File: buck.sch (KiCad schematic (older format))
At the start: 11 parts, among them U2 MP2467

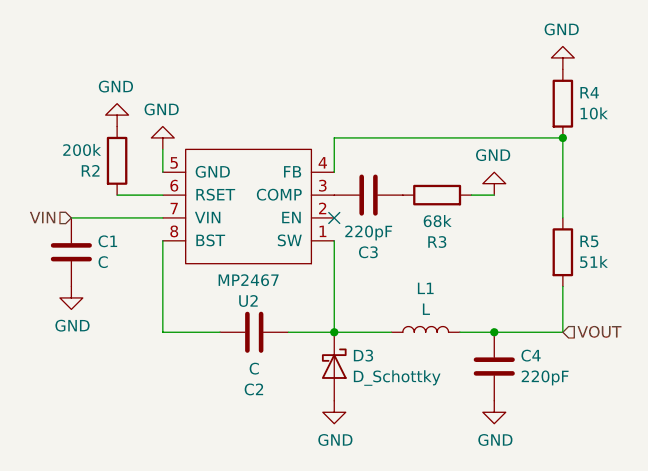
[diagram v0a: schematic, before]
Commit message: Batteries done and raspi added
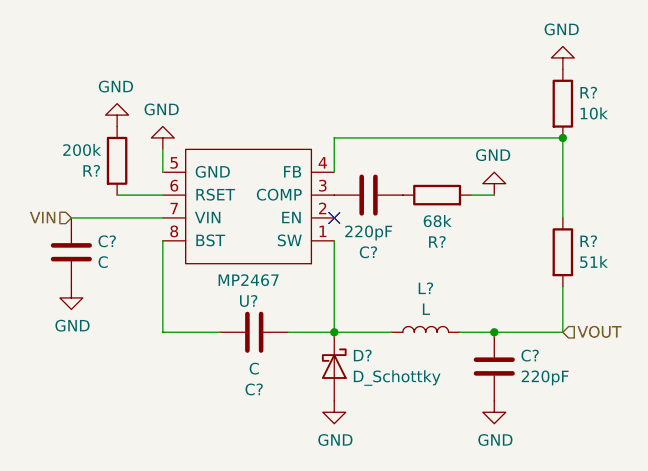
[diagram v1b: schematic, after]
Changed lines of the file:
@@
 $Descr A4 11693 8268
 encoding utf-8
-Sheet 2 7
+Sheet 2 14
 Title ""
 Date ""
@@
 AR Path="/5BDB6444/5BDB68AC" Ref="U2"  Part="1"
 AR Path="/5BE5CA5D/5BDB68AC" Ref="U?"  Part="1"
-F 0 "U2" H 5775 3915 50  0000 C CNN
+AR Path="/5C45D14E/5BDB68AC" Ref="U?"  Part="1"
+F 0 "U?" H 5775 3915 50  0000 C CNN
 F 1 "MP2467" H 5775 3824 50  0000 C CNN
 F 2 "" H 5750 3800 50  0001 C CNN
@@
 AR Path="/5BDB6444/5BDB68B3" Ref="#PWR08"  Part="1"
 AR Path="/5BE5CA5D/5BDB68B3" Ref="#PWR?"  Part="1"
-F 0 "#PWR08" H 4450 3000 50  0001 C CNN
+AR Path="/5C45D14E/5BDB68B3" Ref="#PWR?"  Part="1"
+F 0 "#PWR?" H 4450 3000 50  0001 C CNN
 F 1 "GND" H 4455 3077 50  0000 C CNN
 F 2 "" H 4450 3250 50  0001 C CNN
@@
 AR Path="/5BDB6444/5BDB68B9" Ref="C2"  Part="1"
 AR Path="/5BE5CA5D/5BDB68B9" Ref="C?"  Part="1"
-F 0 "C2" V 4598 4050 50  0000 C CNN
+AR Path="/5C45D14E/5BDB68B9" Ref="C?"  Part="1"
+F 0 "C?" V 4598 4050 50  0000 C CNN
 F 1 "C" V 4689 4050 50  0000 C CNN
 F 2 "" H 4888 3900 50  0001 C CNN
@@
 AR Path="/5BDB6444/5BDB68C4" Ref="C1"  Part="1"
 AR Path="/5BE5CA5D/5BDB68C4" Ref="C?"  Part="1"
-F 0 "C1" H 4165 3746 50  0000 L CNN
+AR Path="/5C45D14E/5BDB68C4" Ref="C?"  Part="1"
+F 0 "C?" H 4165 3746 50  0000 L CNN
 F 1 "C" H 4165 3655 50  0000 L CNN
 F 2 "" H 4088 3550 50  0001 C CNN
@@
 AR Path="/5BDB6444/5BDB68CB" Ref="#PWR06"  Part="1"
 AR Path="/5BE5CA5D/5BDB68CB" Ref="#PWR?"  Part="1"
-F 0 "#PWR06" H 4050 3600 50  0001 C CNN
+AR Path="/5C45D14E/5BDB68CB" Ref="#PWR?"  Part="1"
+F 0 "#PWR?" H 4050 3600 50  0001 C CNN
 F 1 "GND" H 4055 3677 50  0000 C CNN
 F 2 "" H 4050 3850 50  0001 C CNN
@@
 AR Path="/5BDB6444/5BDB68D2" Ref="C3"  Part="1"
 AR Path="/5BE5CA5D/5BDB68D2" Ref="C?"  Part="1"
-F 0 "C3" V 5098 3450 50  0000 C CNN
+AR Path="/5C45D14E/5BDB68D2" Ref="C?"  Part="1"
+F 0 "C?" V 5098 3450 50  0000 C CNN
 F 1 "220pF" V 5189 3450 50  0000 C CNN
 F 2 "" H 5388 3300 50  0001 C CNN
@@
 AR Path="/5BDB6444/5BDB68D9" Ref="R3"  Part="1"
 AR Path="/5BE5CA5D/5BDB68D9" Ref="R?"  Part="1"
-F 0 "R3" V 5443 3450 50  0000 C CNN
+AR Path="/5C45D14E/5BDB68D9" Ref="R?"  Part="1"
+F 0 "R?" V 5443 3450 50  0000 C CNN
 F 1 "68k" V 5534 3450 50  0000 C CNN
 F 2 "" V 5580 3450 50  0001 C CNN
@@
 AR Path="/5BDB6444/5BDB68E0" Ref="#PWR010"  Part="1"
 AR Path="/5BE5CA5D/5BDB68E0" Ref="#PWR?"  Part="1"
-F 0 "#PWR010" H 5900 3200 50  0001 C CNN
+AR Path="/5C45D14E/5BDB68E0" Ref="#PWR?"  Part="1"
+F 0 "#PWR?" H 5900 3200 50  0001 C CNN
 F 1 "GND" H 5905 3277 50  0000 C CNN
 F 2 "" H 5900 3450 50  0001 C CNN
@@
 AR Path="/5BDB6444/5BDB68E7" Ref="R2"  Part="1"
 AR Path="/5BE5CA5D/5BDB68E7" Ref="R?"  Part="1"
-F 0 "R2" H 4180 3254 50  0000 R CNN
+AR Path="/5C45D14E/5BDB68E7" Ref="R?"  Part="1"
+F 0 "R?" H 4180 3254 50  0000 R CNN
 F 1 "200k" H 4180 3345 50  0000 R CNN
 F 2 "" V 4180 3300 50  0001 C CNN
@@
 AR Path="/5BDB6444/5BDB68EF" Ref="#PWR07"  Part="1"
 AR Path="/5BE5CA5D/5BDB68EF" Ref="#PWR?"  Part="1"
-F 0 "#PWR07" H 4250 2900 50  0001 C CNN
+AR Path="/5C45D14E/5BDB68EF" Ref="#PWR?"  Part="1"
+F 0 "#PWR?" H 4250 2900 50  0001 C CNN
 F 1 "GND" H 4255 2977 50  0000 C CNN
 F 2 "" H 4250 3150 50  0001 C CNN
@@
 AR Path="/5BDB6444/5BDB68F6" Ref="D3"  Part="1"
 AR Path="/5BE5CA5D/5BDB68F6" Ref="D?"  Part="1"
-F 0 "D3" V 5154 4279 50  0000 L CNN
+AR Path="/5C45D14E/5BDB68F6" Ref="D?"  Part="1"
+F 0 "D?" V 5154 4279 50  0000 L CNN
 F 1 "D_Schottky" V 5245 4279 50  0000 L CNN
 F 2 "" H 5200 4200 50  0001 C CNN
@@
 AR Path="/5BDB6444/5BDB68FE" Ref="#PWR09"  Part="1"
 AR Path="/5BE5CA5D/5BDB68FE" Ref="#PWR?"  Part="1"
-F 0 "#PWR09" H 5200 4100 50  0001 C CNN
+AR Path="/5C45D14E/5BDB68FE" Ref="#PWR?"  Part="1"
+F 0 "#PWR?" H 5200 4100 50  0001 C CNN
 F 1 "GND" H 5205 4177 50  0000 C CNN
 F 2 "" H 5200 4350 50  0001 C CNN
@@
 AR Path="/5BDB6444/5BDB6904" Ref="L1"  Part="1"
 AR Path="/5BE5CA5D/5BDB6904" Ref="L?"  Part="1"
-F 0 "L1" V 5790 4050 50  0000 C CNN
+AR Path="/5C45D14E/5BDB6904" Ref="L?"  Part="1"
+F 0 "L?" V 5790 4050 50  0000 C CNN
 F 1 "L" V 5699 4050 50  0000 C CNN
 F 2 "" H 5600 4050 50  0001 C CNN
@@
 AR Path="/5BDB6444/5BDB690C" Ref="C4"  Part="1"
 AR Path="/5BE5CA5D/5BDB690C" Ref="C?"  Part="1"
-F 0 "C4" H 6015 4246 50  0000 L CNN
+AR Path="/5C45D14E/5BDB690C" Ref="C?"  Part="1"
+F 0 "C?" H 6015 4246 50  0000 L CNN
 F 1 "220pF" H 6015 4155 50  0000 L CNN
 F 2 "" H 5938 4050 50  0001 C CNN
@@
 AR Path="/5BDB6444/5BDB6913" Ref="#PWR011"  Part="1"
 AR Path="/5BE5CA5D/5BDB6913" Ref="#PWR?"  Part="1"
-F 0 "#PWR011" H 5900 4100 50  0001 C CNN
+AR Path="/5C45D14E/5BDB6913" Ref="#PWR?"  Part="1"
+F 0 "#PWR?" H 5900 4100 50  0001 C CNN
 F 1 "GND" H 5905 4177 50  0000 C CNN
 F 2 "" H 5900 4350 50  0001 C CNN
@@
 AR Path="/5BDB6444/5BDB691A" Ref="R5"  Part="1"
 AR Path="/5BE5CA5D/5BDB691A" Ref="R?"  Part="1"
-F 0 "R5" H 6270 3746 50  0000 L CNN
+AR Path="/5C45D14E/5BDB691A" Ref="R?"  Part="1"
+F 0 "R?" H 6270 3746 50  0000 L CNN
 F 1 "51k" H 6270 3655 50  0000 L CNN
 F 2 "" V 6130 3700 50  0001 C CNN
@@
 AR Path="/5BDB6444/5BDB6921" Ref="R4"  Part="1"
 AR Path="/5BE5CA5D/5BDB6921" Ref="R?"  Part="1"
-F 0 "R4" H 6270 3096 50  0000 L CNN
+AR Path="/5C45D14E/5BDB6921" Ref="R?"  Part="1"
+F 0 "R?" H 6270 3096 50  0000 L CNN
 F 1 "10k" H 6270 3005 50  0000 L CNN
 F 2 "" V 6130 3050 50  0001 C CNN
@@
 AR Path="/5BDB6444/5BDB692F" Ref="#PWR012"  Part="1"
 AR Path="/5BE5CA5D/5BDB692F" Ref="#PWR?"  Part="1"
-F 0 "#PWR012" H 6200 2650 50  0001 C CNN
+AR Path="/5C45D14E/5BDB692F" Ref="#PWR?"  Part="1"
+F 0 "#PWR?" H 6200 2650 50  0001 C CNN
 F 1 "GND" H 6205 2727 50  0000 C CNN
 F 2 "" H 6200 2900 50  0001 C CNN

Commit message: Schematics Done. Now need to do footprints
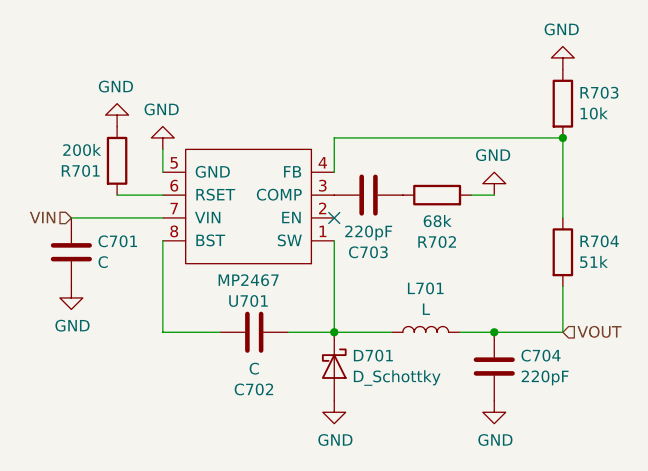
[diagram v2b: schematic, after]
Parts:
- R2, R3, R4, R5: footprint (none) -> Resistor_SMD:R_0805_2012Metric
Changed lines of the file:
@@
 AR Path="/5BDB6444/5BDB68AC" Ref="U2"  Part="1"
 AR Path="/5BE5CA5D/5BDB68AC" Ref="U?"  Part="1"
-AR Path="/5C45D14E/5BDB68AC" Ref="U?"  Part="1"
-F 0 "U?" H 5775 3915 50  0000 C CNN
+AR Path="/5C45D14E/5BDB68AC" Ref="U701"  Part="1"
+F 0 "U701" H 5775 3915 50  0000 C CNN
 F 1 "MP2467" H 5775 3824 50  0000 C CNN
 F 2 "" H 5750 3800 50  0001 C CNN
@@
 AR Path="/5BDB6444/5BDB68B3" Ref="#PWR08"  Part="1"
 AR Path="/5BE5CA5D/5BDB68B3" Ref="#PWR?"  Part="1"
-AR Path="/5C45D14E/5BDB68B3" Ref="#PWR?"  Part="1"
-F 0 "#PWR?" H 4450 3000 50  0001 C CNN
+AR Path="/5C45D14E/5BDB68B3" Ref="#PWR0181"  Part="1"
+F 0 "#PWR0181" H 4450 3000 50  0001 C CNN
 F 1 "GND" H 4455 3077 50  0000 C CNN
 F 2 "" H 4450 3250 50  0001 C CNN
@@
 AR Path="/5BDB6444/5BDB68B9" Ref="C2"  Part="1"
 AR Path="/5BE5CA5D/5BDB68B9" Ref="C?"  Part="1"
-AR Path="/5C45D14E/5BDB68B9" Ref="C?"  Part="1"
-F 0 "C?" V 4598 4050 50  0000 C CNN
+AR Path="/5C45D14E/5BDB68B9" Ref="C702"  Part="1"
+F 0 "C702" V 4598 4050 50  0000 C CNN
 F 1 "C" V 4689 4050 50  0000 C CNN
 F 2 "" H 4888 3900 50  0001 C CNN
@@
 AR Path="/5BDB6444/5BDB68C4" Ref="C1"  Part="1"
 AR Path="/5BE5CA5D/5BDB68C4" Ref="C?"  Part="1"
-AR Path="/5C45D14E/5BDB68C4" Ref="C?"  Part="1"
-F 0 "C?" H 4165 3746 50  0000 L CNN
+AR Path="/5C45D14E/5BDB68C4" Ref="C701"  Part="1"
+F 0 "C701" H 4165 3746 50  0000 L CNN
 F 1 "C" H 4165 3655 50  0000 L CNN
 F 2 "" H 4088 3550 50  0001 C CNN
@@
 AR Path="/5BDB6444/5BDB68CB" Ref="#PWR06"  Part="1"
 AR Path="/5BE5CA5D/5BDB68CB" Ref="#PWR?"  Part="1"
-AR Path="/5C45D14E/5BDB68CB" Ref="#PWR?"  Part="1"
-F 0 "#PWR?" H 4050 3600 50  0001 C CNN
+AR Path="/5C45D14E/5BDB68CB" Ref="#PWR0182"  Part="1"
+F 0 "#PWR0182" H 4050 3600 50  0001 C CNN
 F 1 "GND" H 4055 3677 50  0000 C CNN
 F 2 "" H 4050 3850 50  0001 C CNN
@@
 AR Path="/5BDB6444/5BDB68D2" Ref="C3"  Part="1"
 AR Path="/5BE5CA5D/5BDB68D2" Ref="C?"  Part="1"
-AR Path="/5C45D14E/5BDB68D2" Ref="C?"  Part="1"
-F 0 "C?" V 5098 3450 50  0000 C CNN
+AR Path="/5C45D14E/5BDB68D2" Ref="C703"  Part="1"
+F 0 "C703" V 5098 3450 50  0000 C CNN
 F 1 "220pF" V 5189 3450 50  0000 C CNN
 F 2 "" H 5388 3300 50  0001 C CNN
@@
 AR Path="/5BDB6444/5BDB68D9" Ref="R3"  Part="1"
 AR Path="/5BE5CA5D/5BDB68D9" Ref="R?"  Part="1"
-AR Path="/5C45D14E/5BDB68D9" Ref="R?"  Part="1"
-F 0 "R?" V 5443 3450 50  0000 C CNN
+AR Path="/5C45D14E/5BDB68D9" Ref="R702"  Part="1"
+F 0 "R702" V 5443 3450 50  0000 C CNN
 F 1 "68k" V 5534 3450 50  0000 C CNN
-F 2 "" V 5580 3450 50  0001 C CNN
+F 2 "Resistor_SMD:R_0805_2012Metric" V 5580 3450 50  0001 C CNN
 F 3 "~" H 5650 3450 50  0001 C CNN
 	1    5650 3450
@@
 AR Path="/5BDB6444/5BDB68E0" Ref="#PWR010"  Part="1"
 AR Path="/5BE5CA5D/5BDB68E0" Ref="#PWR?"  Part="1"
-AR Path="/5C45D14E/5BDB68E0" Ref="#PWR?"  Part="1"
-F 0 "#PWR?" H 5900 3200 50  0001 C CNN
+AR Path="/5C45D14E/5BDB68E0" Ref="#PWR0183"  Part="1"
+F 0 "#PWR0183" H 5900 3200 50  0001 C CNN
 F 1 "GND" H 5905 3277 50  0000 C CNN
 F 2 "" H 5900 3450 50  0001 C CNN
@@
 AR Path="/5BDB6444/5BDB68E7" Ref="R2"  Part="1"
 AR Path="/5BE5CA5D/5BDB68E7" Ref="R?"  Part="1"
-AR Path="/5C45D14E/5BDB68E7" Ref="R?"  Part="1"
-F 0 "R?" H 4180 3254 50  0000 R CNN
+AR Path="/5C45D14E/5BDB68E7" Ref="R701"  Part="1"
+F 0 "R701" H 4180 3254 50  0000 R CNN
 F 1 "200k" H 4180 3345 50  0000 R CNN
-F 2 "" V 4180 3300 50  0001 C CNN
+F 2 "Resistor_SMD:R_0805_2012Metric" V 4180 3300 50  0001 C CNN
 F 3 "~" H 4250 3300 50  0001 C CNN
 	1    4250 3300
@@
 AR Path="/5BDB6444/5BDB68EF" Ref="#PWR07"  Part="1"
 AR Path="/5BE5CA5D/5BDB68EF" Ref="#PWR?"  Part="1"
-AR Path="/5C45D14E/5BDB68EF" Ref="#PWR?"  Part="1"
-F 0 "#PWR?" H 4250 2900 50  0001 C CNN
+AR Path="/5C45D14E/5BDB68EF" Ref="#PWR0184"  Part="1"
+F 0 "#PWR0184" H 4250 2900 50  0001 C CNN
 F 1 "GND" H 4255 2977 50  0000 C CNN
 F 2 "" H 4250 3150 50  0001 C CNN
@@
 AR Path="/5BDB6444/5BDB68F6" Ref="D3"  Part="1"
 AR Path="/5BE5CA5D/5BDB68F6" Ref="D?"  Part="1"
-AR Path="/5C45D14E/5BDB68F6" Ref="D?"  Part="1"
-F 0 "D?" V 5154 4279 50  0000 L CNN
+AR Path="/5C45D14E/5BDB68F6" Ref="D701"  Part="1"
+F 0 "D701" V 5154 4279 50  0000 L CNN
 F 1 "D_Schottky" V 5245 4279 50  0000 L CNN
 F 2 "" H 5200 4200 50  0001 C CNN
@@
 AR Path="/5BDB6444/5BDB68FE" Ref="#PWR09"  Part="1"
 AR Path="/5BE5CA5D/5BDB68FE" Ref="#PWR?"  Part="1"
-AR Path="/5C45D14E/5BDB68FE" Ref="#PWR?"  Part="1"
-F 0 "#PWR?" H 5200 4100 50  0001 C CNN
+AR Path="/5C45D14E/5BDB68FE" Ref="#PWR0185"  Part="1"
+F 0 "#PWR0185" H 5200 4100 50  0001 C CNN
 F 1 "GND" H 5205 4177 50  0000 C CNN
 F 2 "" H 5200 4350 50  0001 C CNN
@@
 AR Path="/5BDB6444/5BDB6904" Ref="L1"  Part="1"
 AR Path="/5BE5CA5D/5BDB6904" Ref="L?"  Part="1"
-AR Path="/5C45D14E/5BDB6904" Ref="L?"  Part="1"
-F 0 "L?" V 5790 4050 50  0000 C CNN
+AR Path="/5C45D14E/5BDB6904" Ref="L701"  Part="1"
+F 0 "L701" V 5790 4050 50  0000 C CNN
 F 1 "L" V 5699 4050 50  0000 C CNN
 F 2 "" H 5600 4050 50  0001 C CNN
@@
 AR Path="/5BDB6444/5BDB690C" Ref="C4"  Part="1"
 AR Path="/5BE5CA5D/5BDB690C" Ref="C?"  Part="1"
-AR Path="/5C45D14E/5BDB690C" Ref="C?"  Part="1"
-F 0 "C?" H 6015 4246 50  0000 L CNN
+AR Path="/5C45D14E/5BDB690C" Ref="C704"  Part="1"
+F 0 "C704" H 6015 4246 50  0000 L CNN
 F 1 "220pF" H 6015 4155 50  0000 L CNN
 F 2 "" H 5938 4050 50  0001 C CNN
@@
 AR Path="/5BDB6444/5BDB6913" Ref="#PWR011"  Part="1"
 AR Path="/5BE5CA5D/5BDB6913" Ref="#PWR?"  Part="1"
-AR Path="/5C45D14E/5BDB6913" Ref="#PWR?"  Part="1"
-F 0 "#PWR?" H 5900 4100 50  0001 C CNN
+AR Path="/5C45D14E/5BDB6913" Ref="#PWR0186"  Part="1"
+F 0 "#PWR0186" H 5900 4100 50  0001 C CNN
 F 1 "GND" H 5905 4177 50  0000 C CNN
 F 2 "" H 5900 4350 50  0001 C CNN
@@
 AR Path="/5BDB6444/5BDB691A" Ref="R5"  Part="1"
 AR Path="/5BE5CA5D/5BDB691A" Ref="R?"  Part="1"
-AR Path="/5C45D14E/5BDB691A" Ref="R?"  Part="1"
-F 0 "R?" H 6270 3746 50  0000 L CNN
+AR Path="/5C45D14E/5BDB691A" Ref="R704"  Part="1"
+F 0 "R704" H 6270 3746 50  0000 L CNN
 F 1 "51k" H 6270 3655 50  0000 L CNN
-F 2 "" V 6130 3700 50  0001 C CNN
+F 2 "Resistor_SMD:R_0805_2012Metric" V 6130 3700 50  0001 C CNN
 F 3 "~" H 6200 3700 50  0001 C CNN
 	1    6200 3700
@@
 AR Path="/5BDB6444/5BDB6921" Ref="R4"  Part="1"
 AR Path="/5BE5CA5D/5BDB6921" Ref="R?"  Part="1"
-AR Path="/5C45D14E/5BDB6921" Ref="R?"  Part="1"
-F 0 "R?" H 6270 3096 50  0000 L CNN
+AR Path="/5C45D14E/5BDB6921" Ref="R703"  Part="1"
+F 0 "R703" H 6270 3096 50  0000 L CNN
 F 1 "10k" H 6270 3005 50  0000 L CNN
-F 2 "" V 6130 3050 50  0001 C CNN
+F 2 "Resistor_SMD:R_0805_2012Metric" V 6130 3050 50  0001 C CNN
 F 3 "~" H 6200 3050 50  0001 C CNN
 	1    6200 3050
@@
 AR Path="/5BDB6444/5BDB692F" Ref="#PWR012"  Part="1"
 AR Path="/5BE5CA5D/5BDB692F" Ref="#PWR?"  Part="1"
-AR Path="/5C45D14E/5BDB692F" Ref="#PWR?"  Part="1"
-F 0 "#PWR?" H 6200 2650 50  0001 C CNN
+AR Path="/5C45D14E/5BDB692F" Ref="#PWR0187"  Part="1"
+F 0 "#PWR0187" H 6200 2650 50  0001 C CNN
 F 1 "GND" H 6205 2727 50  0000 C CNN
 F 2 "" H 6200 2900 50  0001 C CNN

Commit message: Schematics done, now assigning footprints to do PCB Next
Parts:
- C1, C2, C3, C4: footprint (none) -> Capacitor_SMD:C_0805_2012Metric
- D3: footprint (none) -> Diode_SMD:D_0805_2012Metric
- L1: footprint (none) -> Inductor_SMD:L_0805_2012Metric
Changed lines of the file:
@@
 F 0 "C702" V 4598 4050 50  0000 C CNN
 F 1 "C" V 4689 4050 50  0000 C CNN
-F 2 "" H 4888 3900 50  0001 C CNN
+F 2 "Capacitor_SMD:C_0805_2012Metric" H 4888 3900 50  0001 C CNN
 F 3 "~" H 4850 4050 50  0001 C CNN
 	1    4850 4050
@@
 F 0 "C701" H 4165 3746 50  0000 L CNN
 F 1 "C" H 4165 3655 50  0000 L CNN
-F 2 "" H 4088 3550 50  0001 C CNN
+F 2 "Capacitor_SMD:C_0805_2012Metric" H 4088 3550 50  0001 C CNN
 F 3 "~" H 4050 3700 50  0001 C CNN
 	1    4050 3700
@@
 F 0 "C703" V 5098 3450 50  0000 C CNN
 F 1 "220pF" V 5189 3450 50  0000 C CNN
-F 2 "" H 5388 3300 50  0001 C CNN
+F 2 "Capacitor_SMD:C_0805_2012Metric" H 5388 3300 50  0001 C CNN
 F 3 "~" H 5350 3450 50  0001 C CNN
 	1    5350 3450
@@
 F 0 "D701" V 5154 4279 50  0000 L CNN
 F 1 "D_Schottky" V 5245 4279 50  0000 L CNN
-F 2 "" H 5200 4200 50  0001 C CNN
+F 2 "Diode_SMD:D_0805_2012Metric" H 5200 4200 50  0001 C CNN
 F 3 "~" H 5200 4200 50  0001 C CNN
 	1    5200 4200
@@
 F 0 "L701" V 5790 4050 50  0000 C CNN
 F 1 "L" V 5699 4050 50  0000 C CNN
-F 2 "" H 5600 4050 50  0001 C CNN
+F 2 "Inductor_SMD:L_0805_2012Metric" H 5600 4050 50  0001 C CNN
 F 3 "~" H 5600 4050 50  0001 C CNN
 	1    5600 4050
@@
 F 0 "C704" H 6015 4246 50  0000 L CNN
 F 1 "220pF" H 6015 4155 50  0000 L CNN
-F 2 "" H 5938 4050 50  0001 C CNN
+F 2 "Capacitor_SMD:C_0805_2012Metric" H 5938 4050 50  0001 C CNN
 F 3 "~" H 5900 4200 50  0001 C CNN
 	1    5900 4200

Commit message: Assigning footprints
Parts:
- U2: footprint (none) -> Package_SO:SOIC-8_3.9x4.9mm_P1.27mm
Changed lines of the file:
@@
 F 0 "U701" H 5775 3915 50  0000 C CNN
 F 1 "MP2467" H 5775 3824 50  0000 C CNN
-F 2 "" H 5750 3800 50  0001 C CNN
+F 2 "Package_SO:SOIC-8_3.9x4.9mm_P1.27mm" H 5750 3800 50  0001 C CNN
 F 3 "" H 5750 3800 50  0001 C CNN
 	1    5300 4250

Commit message: updated layout
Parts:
- U2: symbol Converter_ACDC:MP2467 -> Mars-Rover-rescue:MP2467-Converter_ACDC
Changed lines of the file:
@@
 $EndDescr
 $Comp
-L Converter_ACDC:MP2467 U?
+L Mars-Rover-rescue:MP2467-Converter_ACDC U?
 U 1 1 5BDB68AC
 P 5300 4250
